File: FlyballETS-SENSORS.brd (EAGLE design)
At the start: 81.3 x 83.8 mm, 42 parts

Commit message: Updated drawings and added PNG exports
- Added frames around drawings to make it look neater
- Added PNG export files so people who don't have EAGLE can see
everything
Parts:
- added U$1: (no value), frames:A5L-LOC
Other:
- board text added: "Alex Goris"
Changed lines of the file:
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@@
 <wire x1="80.01" y1="1.27" x2="48.895" y2="1.27" width="0.4064" layer="21"/>
 <text x="58.42" y="2.54" size="1.778" layer="21">S2: Box Side</text>
+<dimension x1="81.28" y1="0" x2="81.28" y2="83.82" x3="91.44" y3="41.91" textsize="1.778" layer="48"/>
+<dimension x1="81.28" y1="83.82" x2="0" y2="83.82" x3="40.64" y3="93.98" textsize="1.778" layer="48"/>
+<text x="53.34" y="-20.32" size="2.54" layer="48">FlyballETS
+SensorBoard v1
+http://bit.ly/1ErZ5QD
+LICENSE: CC-BY-SA</text>
+<text x="107.95" y="-7.62" size="2.54" layer="48">Alex Goris</text>
 </plain>
 <attributes>
@@
 <element name="S2-9" library="bt_con-jst-xh" package="B3B-XH" value="03-JST-B3B-XH-A" x="76.2" y="48.26" rot="R90"/>
 <element name="SENS" library="bt_con-jst-xh" package="B2B-XH" value="02-JST-B2B-XH-A" x="12.7" y="76.2"/>
+<element name="U$1" library="frames" package="A5L-LOC" value="" x="-33.02" y="-27.94"/>
 </elements>
 <signals>

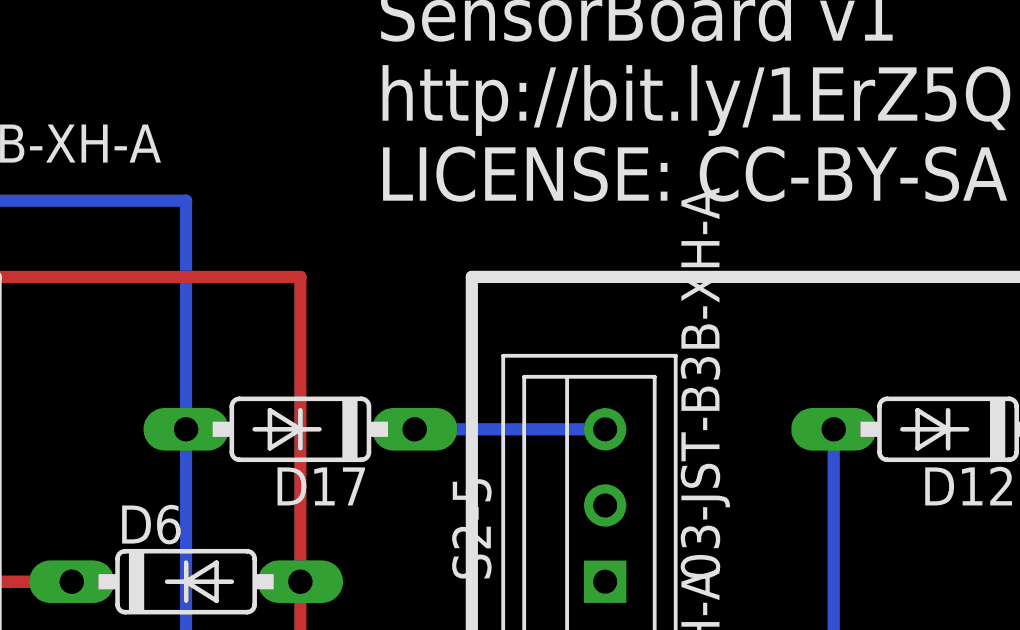
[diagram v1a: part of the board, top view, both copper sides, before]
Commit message: Corrected unrouted airwire
The SensorsBoard had an unrouted airwire, this has been corrected
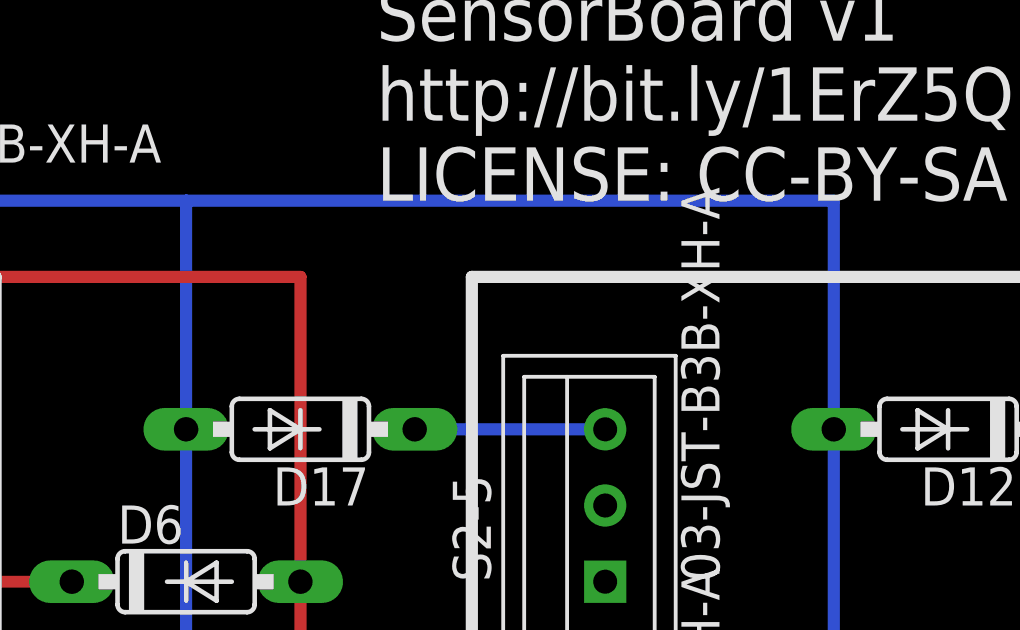
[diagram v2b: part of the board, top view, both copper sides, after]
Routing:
- net S1: track 141.0 -> 170.2 mm
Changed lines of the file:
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@@
 <?xml version="1.0" encoding="utf-8"?>
 <!DOCTYPE eagle SYSTEM "eagle.dtd">
-<eagle version="7.3.0">
+<eagle version="7.4.0">
 <drawing>
 <settings>
@@
 <wire x1="39.37" y1="71.12" x2="12.7" y2="71.12" width="0.4064" layer="16"/>
 <wire x1="12.7" y1="71.12" x2="12.7" y2="76.2" width="0.4064" layer="16"/>
-<wire x1="39.37" y1="63.5" x2="60.96" y2="63.5" width="0" layer="19" extent="1-1"/>
+<wire x1="60.96" y1="63.5" x2="60.96" y2="71.12" width="0.4064" layer="16"/>
+<wire x1="60.96" y1="71.12" x2="39.37" y2="71.12" width="0.4064" layer="16"/>
 </signal>
 <signal name="N$11">

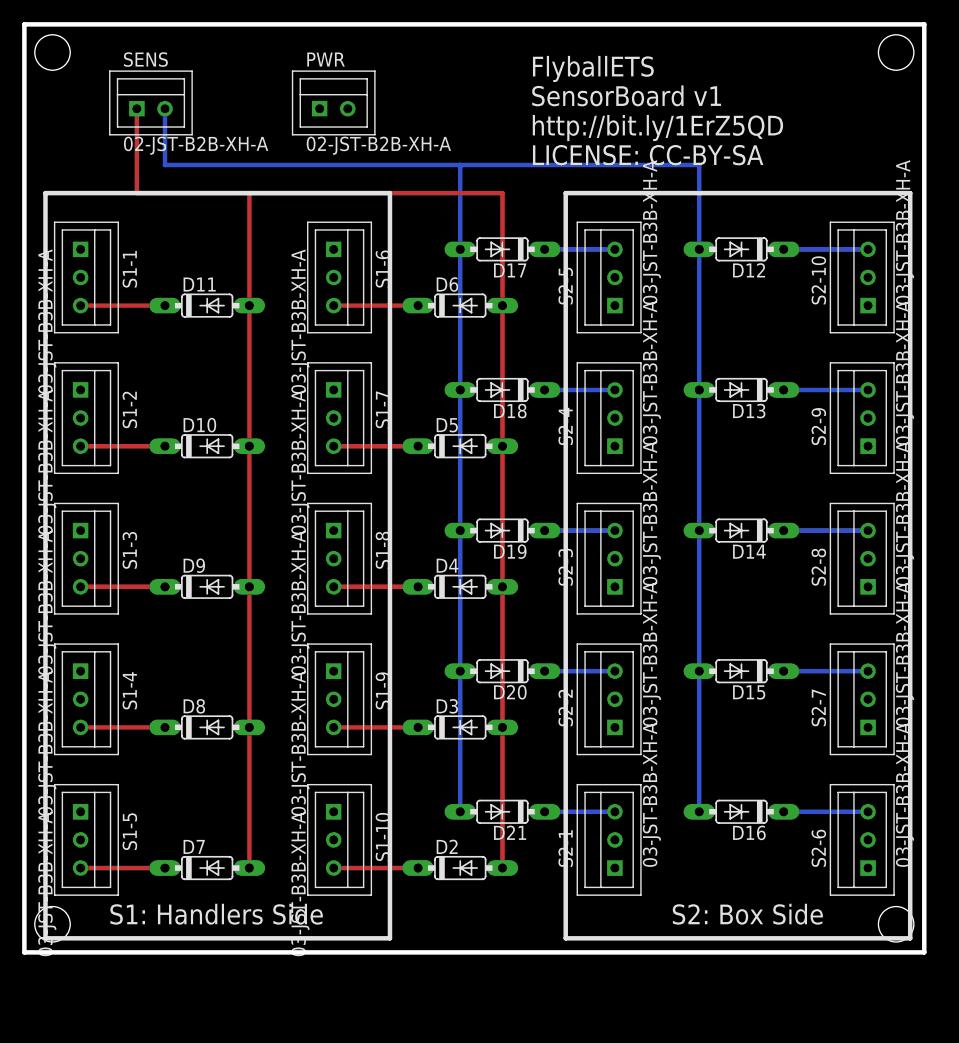
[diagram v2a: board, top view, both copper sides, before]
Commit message: v2 release of remaining boards.
- Lightsboard: Corrected swapped pin connections on L2 side and made
smaller
- Powerboard: Made smaller and added descriptions for LM2596 board
- Sensorboard: Made smaller
- All boards: Removed JST connector type names
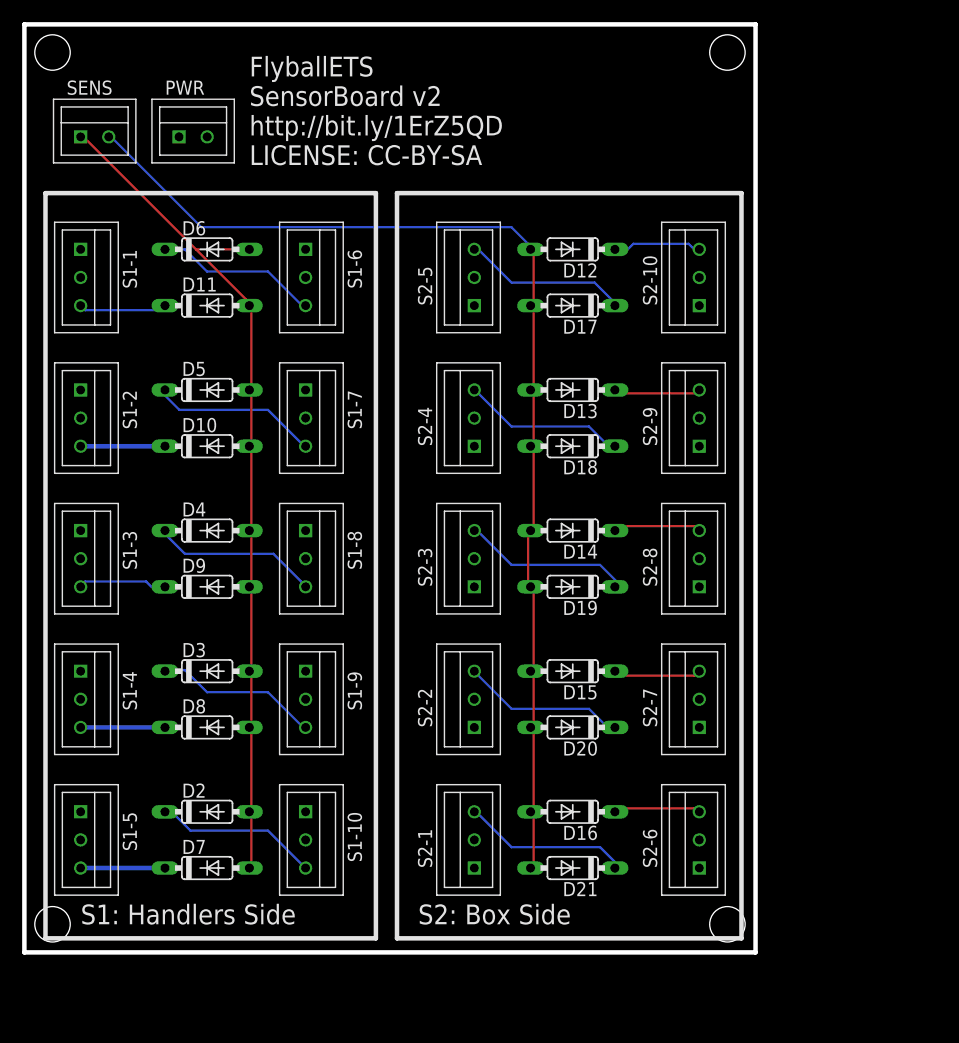
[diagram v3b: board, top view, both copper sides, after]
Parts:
- moved D2 23.4 mm to (16.5, 12.7)
- moved D3 23.4 mm to (16.5, 25.4)
- moved D4 23.4 mm to (16.5, 38.1)
- moved D5 23.4 mm to (16.5, 50.8)
- moved D6 23.4 mm to (16.5, 63.5)
- moved S2-10 15.2 mm to (61.0, 61.0)
- moved S2-6 15.2 mm to (61.0, 10.2)
- moved S2-7 15.2 mm to (61.0, 22.9)
- moved S2-8 15.2 mm to (61.0, 35.6)
- moved S2-9 15.2 mm to (61.0, 48.3)
- moved D12 15.2 mm to (49.5, 63.5)
- moved D13 15.2 mm to (49.5, 50.8)
- moved D14 15.2 mm to (49.5, 38.1)
- moved D15 15.2 mm to (49.5, 25.4)
- moved D16 15.2 mm to (49.5, 12.7)
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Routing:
- net S2: track 162.6 -> 78.4 mm
- net S1: track 170.2 -> 101.2 mm
- net N$13: track 6.35 -> 15.2 mm
- net N$11: track 6.35 -> 15.2 mm
- net N$15: track 6.35 -> 15.1 mm
- net N$12: track 6.35 -> 14.8 mm
- net N$14: track 6.35 -> 14.8 mm
- net N$7: track 7.62 -> 15.2 mm
- net N$8: track 7.62 -> 15.2 mm
- net N$9: track 7.62 -> 14.8 mm
- net N$6: track 7.62 -> 14.8 mm
- net N$10: track 7.62 -> 14.8 mm
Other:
- board size 81.3 x 83.8 mm -> 66 x 83.8 mm
- board text added: "FlyballETS SensorBoard v2 http://bit.ly/1ErZ5QD LICENSE: CC-BY-SA"
- board text removed: "FlyballETS SensorBoard v1 http://bit.ly/1ErZ5QD LICENSE: CC-BY-SA"

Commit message: Fixed several issues
- Checked all mounting holes (fixes #1 )
- Marked light colors on lights PCB (fixes #7 )
- Swapped pins 2 and 3 on LIGHTS connected on PWR board (fixes #3 )
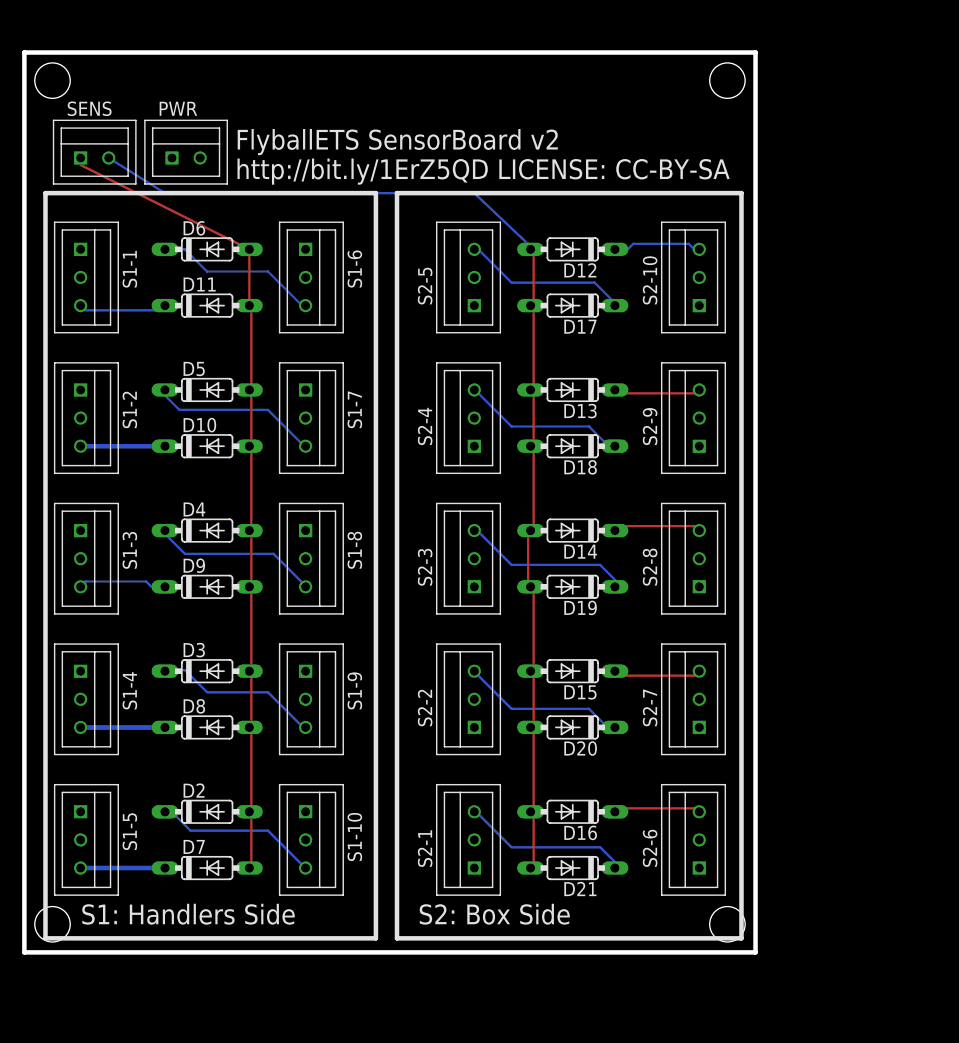
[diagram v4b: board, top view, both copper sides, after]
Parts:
- moved PWR 2.01 mm to (15.9, 71.8)
- moved SENS 1.91 mm to (7.62, 71.8)
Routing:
- net S2: track 78.4 -> 74.6 mm
- net S1: track 101.2 -> 100.0 mm
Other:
- board size 66 x 83.8 mm -> 66 x 81.3 mm
- board text added: "Units: mm"
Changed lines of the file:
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@@
 <board>
 <plain>
-<wire x1="0" y1="0" x2="0" y2="83.82" width="0.4064" layer="20"/>
-<wire x1="0" y1="83.82" x2="66.04" y2="83.82" width="0.4064" layer="20"/>
-<wire x1="66.04" y1="83.82" x2="66.04" y2="0" width="0.4064" layer="20"/>
+<wire x1="0" y1="0" x2="0" y2="81.28" width="0.4064" layer="20"/>
+<wire x1="0" y1="81.28" x2="66.04" y2="81.28" width="0.4064" layer="20"/>
+<wire x1="66.04" y1="81.28" x2="66.04" y2="0" width="0.4064" layer="20"/>
 <wire x1="66.04" y1="0" x2="0" y2="0" width="0.4064" layer="20"/>
-<hole x="2.54" y="81.28" drill="3.2"/>
-<hole x="63.5" y="81.28" drill="3.2"/>
+<hole x="2.54" y="78.74" drill="3.2"/>
+<hole x="63.5" y="78.74" drill="3.2"/>
 <hole x="63.5" y="2.54" drill="3.2"/>
 <hole x="2.54" y="2.54" drill="3.2"/>
-<text x="20.32" y="71.12" size="1.778" layer="21">FlyballETS
-SensorBoard v2
-http://bit.ly/1ErZ5QD
-LICENSE: CC-BY-SA</text>
+<text x="19.05" y="69.85" size="1.778" layer="21">FlyballETS SensorBoard v2
+http://bit.ly/1ErZ5QD LICENSE: CC-BY-SA</text>
 <wire x1="1.905" y1="68.58" x2="31.75" y2="68.58" width="0.4064" layer="21"/>
 <wire x1="31.75" y1="68.58" x2="31.75" y2="1.27" width="0.4064" layer="21"/>
@@
 <wire x1="64.77" y1="1.27" x2="33.655" y2="1.27" width="0.4064" layer="21"/>
 <text x="35.56" y="2.54" size="1.778" layer="21">S2: Box Side</text>
-<dimension x1="66.04" y1="0" x2="66.04" y2="83.82" x3="76.199996875" y3="41.91" textsize="1.778" layer="48"/>
-<dimension x1="66.04" y1="83.82" x2="0" y2="83.82" x3="33.02" y3="93.98" textsize="1.778" layer="48"/>
+<dimension x1="66.04" y1="0" x2="66.04" y2="81.28" x3="76.199996875" y3="40.64" textsize="1.778" layer="48"/>
+<dimension x1="66.04" y1="81.28" x2="0" y2="81.28" x3="33.02" y3="91.439996875" textsize="1.778" layer="48"/>
 <text x="53.34" y="-20.32" size="2.54" layer="48">FlyballETS
 SensorBoard v2
@@
 LICENSE: CC-BY-SA</text>
 <text x="107.95" y="-7.62" size="2.54" layer="48">Alex Goris</text>
+<text x="107.95" y="-22.225" size="1.778" layer="48">Units: mm</text>
 </plain>
 <attributes>
@@
 <attribute name="NAME" x="14.224" y="34.29" size="1.27" layer="25" ratio="10"/>
 </element>
-<element name="PWR" library="bt_con-jst-xh" package="B2B-XH" value="02-JST-B2B-XH-A" x="16.51" y="73.66" smashed="yes">
-<attribute name="NAME" x="12.7" y="77.47" size="1.27" layer="21"/>
+<element name="PWR" library="bt_con-jst-xh" package="B2B-XH" value="02-JST-B2B-XH-A" x="15.875" y="71.755" smashed="yes">
+<attribute name="NAME" x="12.065" y="75.565" size="1.27" layer="21"/>
 </element>
 <element name="S1-1" library="bt_con-jst-xh" package="B3B-XH" value="03-JST-B3B-XH-A" x="5.08" y="60.96" smashed="yes" rot="R270">
@@
 <attribute name="NAME" x="57.15" y="45.72" size="1.27" layer="21" rot="R90"/>
 </element>
-<element name="SENS" library="bt_con-jst-xh" package="B2B-XH" value="02-JST-B2B-XH-A" x="7.62" y="73.66" smashed="yes">
-<attribute name="NAME" x="3.81" y="77.47" size="1.27" layer="21"/>
+<element name="SENS" library="bt_con-jst-xh" package="B2B-XH" value="02-JST-B2B-XH-A" x="7.62" y="71.755" smashed="yes">
+<attribute name="NAME" x="3.81" y="75.565" size="1.27" layer="21"/>
 </element>
 <element name="U$1" library="frames" package="A5L-LOC" value="" x="-33.02" y="-27.94"/>
@@
 <polygon width="0.4064" layer="16">
 <vertex x="0" y="0"/>
-<vertex x="0" y="83.82"/>
-<vertex x="66.04" y="83.82"/>
+<vertex x="0" y="81.28"/>
+<vertex x="66.04" y="81.28"/>
 <vertex x="66.04" y="0"/>
 </polygon>
@@
 <polygon width="0.4064" layer="1">
 <vertex x="0" y="0"/>
-<vertex x="0" y="83.82"/>
-<vertex x="66.04" y="83.82"/>
+<vertex x="0" y="81.28"/>
+<vertex x="66.04" y="81.28"/>
 <vertex x="66.04" y="0"/>
 </polygon>
@@
 <contactref element="D11" pad="A"/>
 <contactref element="SENS" pad="P$1"/>
-<wire x1="20" y1="59" x2="15.5" y2="63.5" width="0.2032" layer="1"/>
-<wire x1="15.5" y1="63.5" x2="5.5" y2="73.5" width="0.2032" layer="1"/>
-<wire x1="20" y1="58.5" x2="20" y2="59" width="0.2032" layer="1"/>
-<wire x1="5.5" y1="73.5" x2="5.08" y2="73.66" width="0.2032" layer="1"/>
-<wire x1="20" y1="58.5" x2="20.32" y2="58.42" width="0.2032" layer="1"/>
-<wire x1="15.5" y1="63.5" x2="20.32" y2="63.5" width="0.2032" layer="1"/>
 <wire x1="20.5" y1="50.5" x2="20.5" y2="46" width="0.2032" layer="1"/>
 <wire x1="20.5" y1="46" x2="20.32" y2="45.72" width="0.2032" layer="1"/>
@@
 <wire x1="20.5" y1="58" x2="20.32" y2="58.42" width="0.2032" layer="1"/>
 <wire x1="20.5" y1="51" x2="20.32" y2="50.8" width="0.2032" layer="1"/>
+<wire x1="20.32" y1="58.42" x2="20.32" y2="63.5" width="0.2032" layer="1"/>
+<wire x1="20.32" y1="63.5" x2="5.08" y2="71.12" width="0.2032" layer="1"/>
+<wire x1="5.08" y1="71.12" x2="5.08" y2="71.755" width="0.2032" layer="1"/>
 </signal>
 <signal name="N$1">
@@
 <wire x1="46" y1="45.5" x2="45.72" y2="45.72" width="0.2032" layer="1"/>
 <wire x1="46" y1="38.5" x2="45.72" y2="38.1" width="0.2032" layer="1"/>
-<wire x1="16" y1="65.5" x2="8" y2="73.5" width="0.2032" layer="16"/>
-<wire x1="44" y1="65.5" x2="16" y2="65.5" width="0.2032" layer="16"/>
-<wire x1="46" y1="63.5" x2="44" y2="65.5" width="0.2032" layer="16"/>
-<wire x1="8" y1="73.5" x2="7.62" y2="73.66" width="0.2032" layer="16"/>
 <wire x1="46" y1="63.5" x2="45.72" y2="63.5" width="0.2032" layer="16"/>
 <wire x1="46" y1="63.5" x2="46" y2="58.5" width="0.2032" layer="1"/>
@@
 <wire x1="46" y1="51" x2="45.72" y2="50.8" width="0.2032" layer="1"/>
 <wire x1="46" y1="58" x2="45.72" y2="58.42" width="0.2032" layer="1"/>
+<wire x1="46" y1="63.5" x2="40.64" y2="68.58" width="0.2032" layer="16"/>
+<wire x1="40.64" y1="68.58" x2="12.7" y2="68.58" width="0.2032" layer="16"/>
+<wire x1="12.7" y1="68.58" x2="7.62" y2="71.755" width="0.2032" layer="16"/>
 </signal>
 <signal name="N$11">

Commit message: Fixed JST XH pin numbering
Updated bt_con-jst-xh.lbr library with swapped pin numbering.
Updated all board designs with updated library so they have the
connectors the right way around
Fixes #4
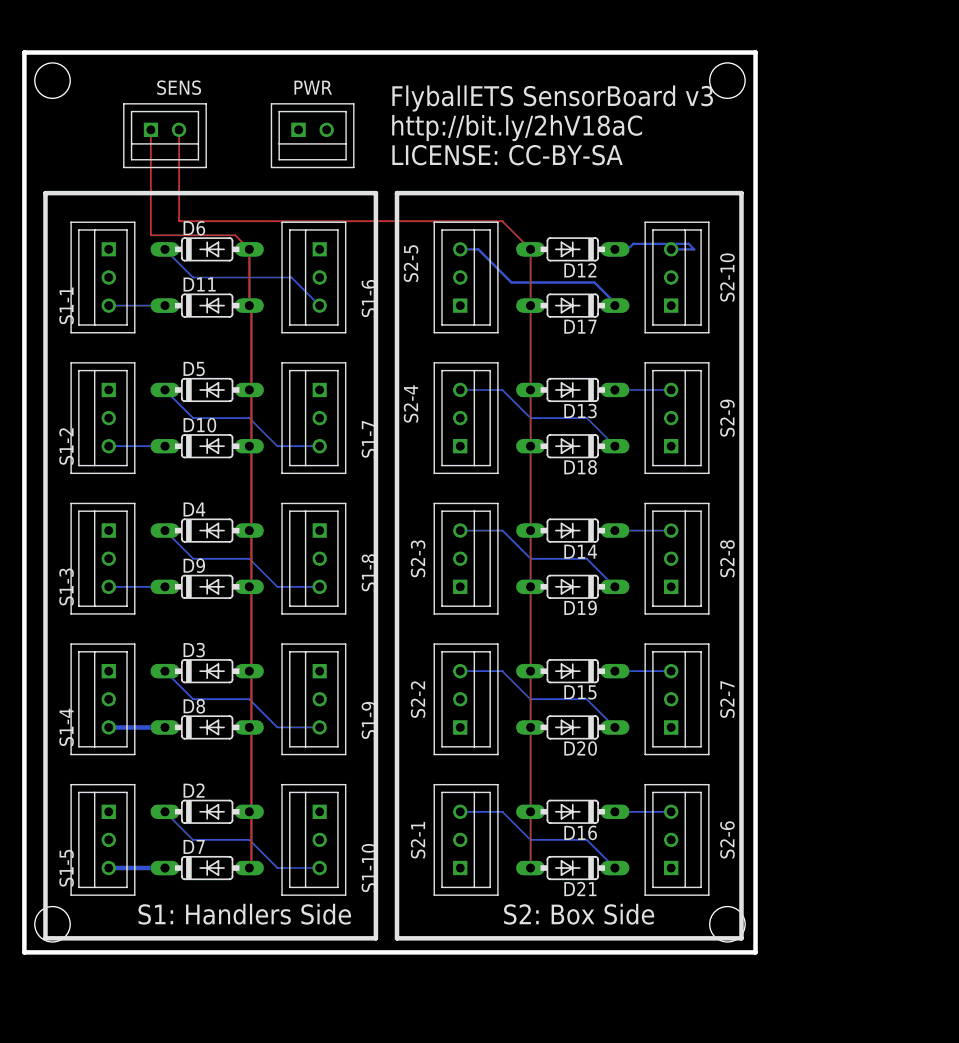
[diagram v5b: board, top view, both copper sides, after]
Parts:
- PWR, SENS: value 02-JST-B2B-XH-A -> 02-JST
- moved PWR 11.7 mm to (27.3, 74.3), turned to 180 degrees
- moved SENS 6.84 mm to (14.0, 74.3), turned to 180 degrees
- moved S1-1 2.54 mm to (7.62, 61.0), turned to 90 degrees
- moved S1-2 2.54 mm to (7.62, 48.3), turned to 90 degrees
- moved S1-3 2.54 mm to (7.62, 35.6), turned to 90 degrees
- moved S1-4 2.54 mm to (7.62, 22.9), turned to 90 degrees
- moved S1-5 2.54 mm to (7.62, 10.2), turned to 90 degrees
- moved S2-10 2.54 mm to (58.4, 61.0), turned to 270 degrees
- moved S2-6 2.54 mm to (58.4, 10.2), turned to 270 degrees
- moved S2-7 2.54 mm to (58.4, 22.9), turned to 270 degrees
- moved S2-8 2.54 mm to (58.4, 35.6), turned to 270 degrees
- moved S2-9 2.54 mm to (58.4, 48.3), turned to 270 degrees
- moved S1-10 1.27 mm to (26.7, 10.2), turned to 90 degrees
- moved S1-6 1.27 mm to (26.7, 61.0), turned to 90 degrees
- moved S1-7 1.27 mm to (26.7, 48.3), turned to 90 degrees
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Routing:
- net S1: track 100.0 -> 97.0 mm
- net N$1: track 8.06 -> 5.08 mm
- net N$3: track 8.05 -> 5.08 mm
- net N$18: track 8.04 -> 5.08 mm
- net N$17: track 8.04 -> 5.08 mm
- net N$16: track 7.89 -> 5.08 mm
- net N$19: track 7.89 -> 5.08 mm
- net N$5: track 7.62 -> 5.08 mm
- net N$4: track 7.62 -> 5.08 mm
- net N$2: track 7.62 -> 5.08 mm
- net N$20: track 8.03 -> 9.65 mm
- net N$14: track 14.8 -> 16.1 mm
- net N$10: track 14.8 -> 16.1 mm
- net N$6: track 14.8 -> 16.1 mm
- net N$12: track 14.8 -> 16.1 mm
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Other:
- board text added: "FlyballETS SensorBoard v3 http://bit.ly/2hV18aC LICENSE: CC-BY-SA"
- board text removed: "FlyballETS SensorBoard v2 http://bit.ly/1ErZ5QD LICENSE: CC-BY-SA"
